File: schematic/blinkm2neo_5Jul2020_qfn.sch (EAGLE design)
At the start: 9 parts, among them IC1 ATTINY85SOIC, J1 blinkm

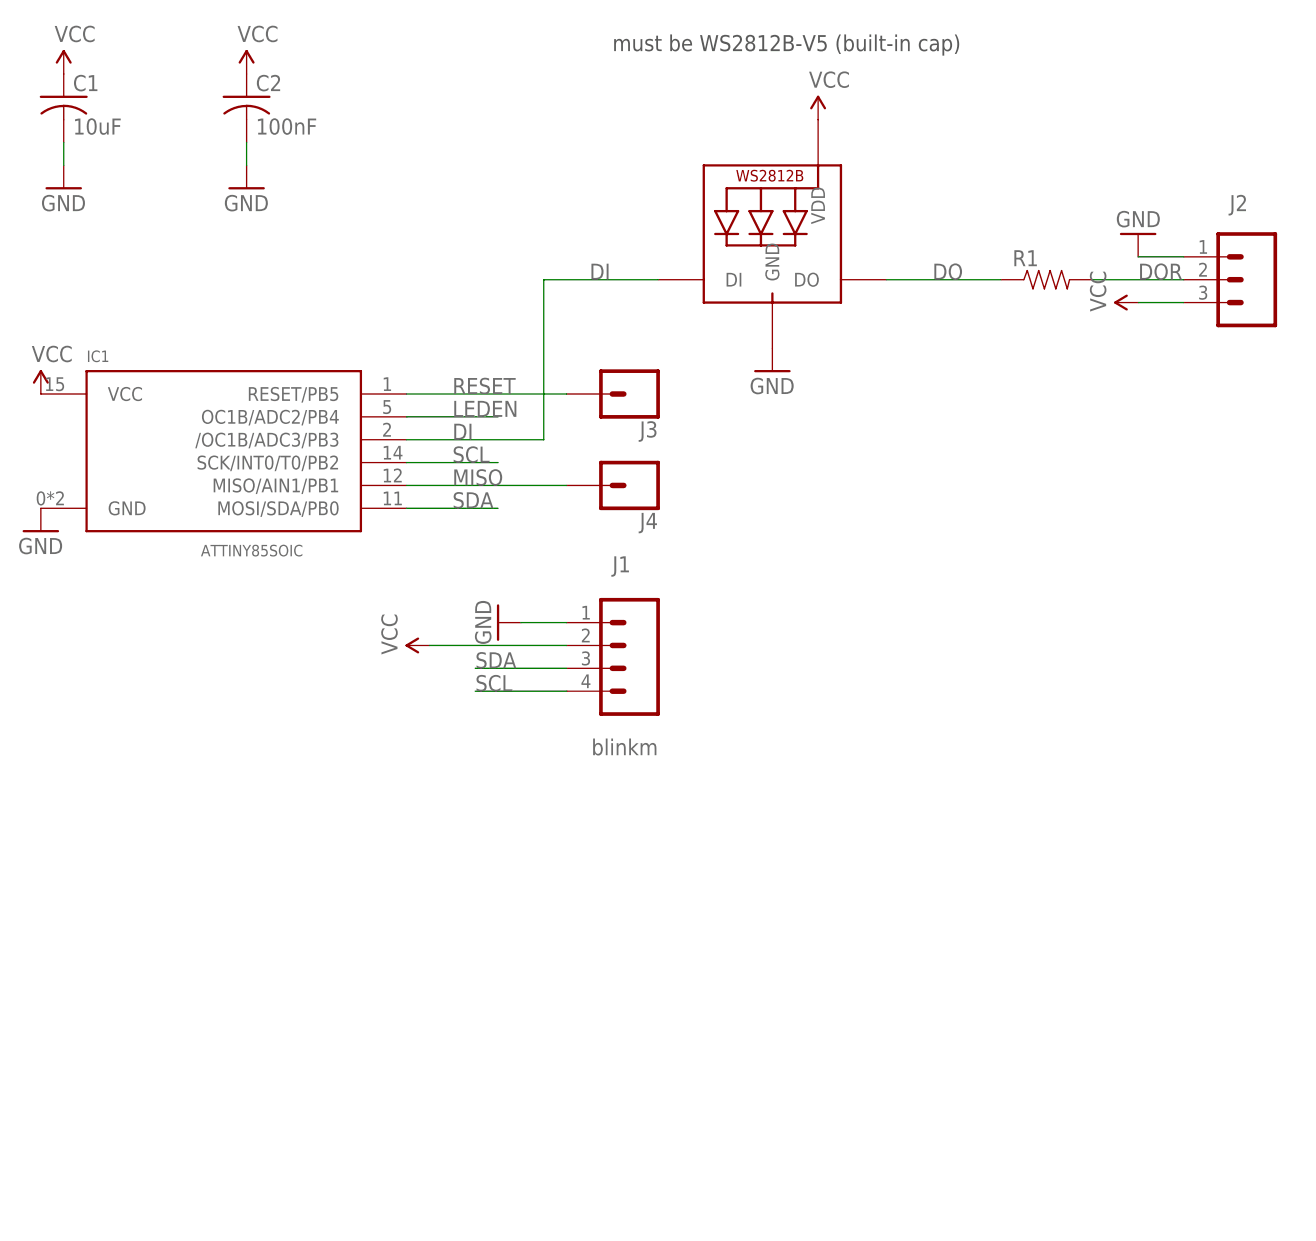
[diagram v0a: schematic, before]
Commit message: added pullup resistors
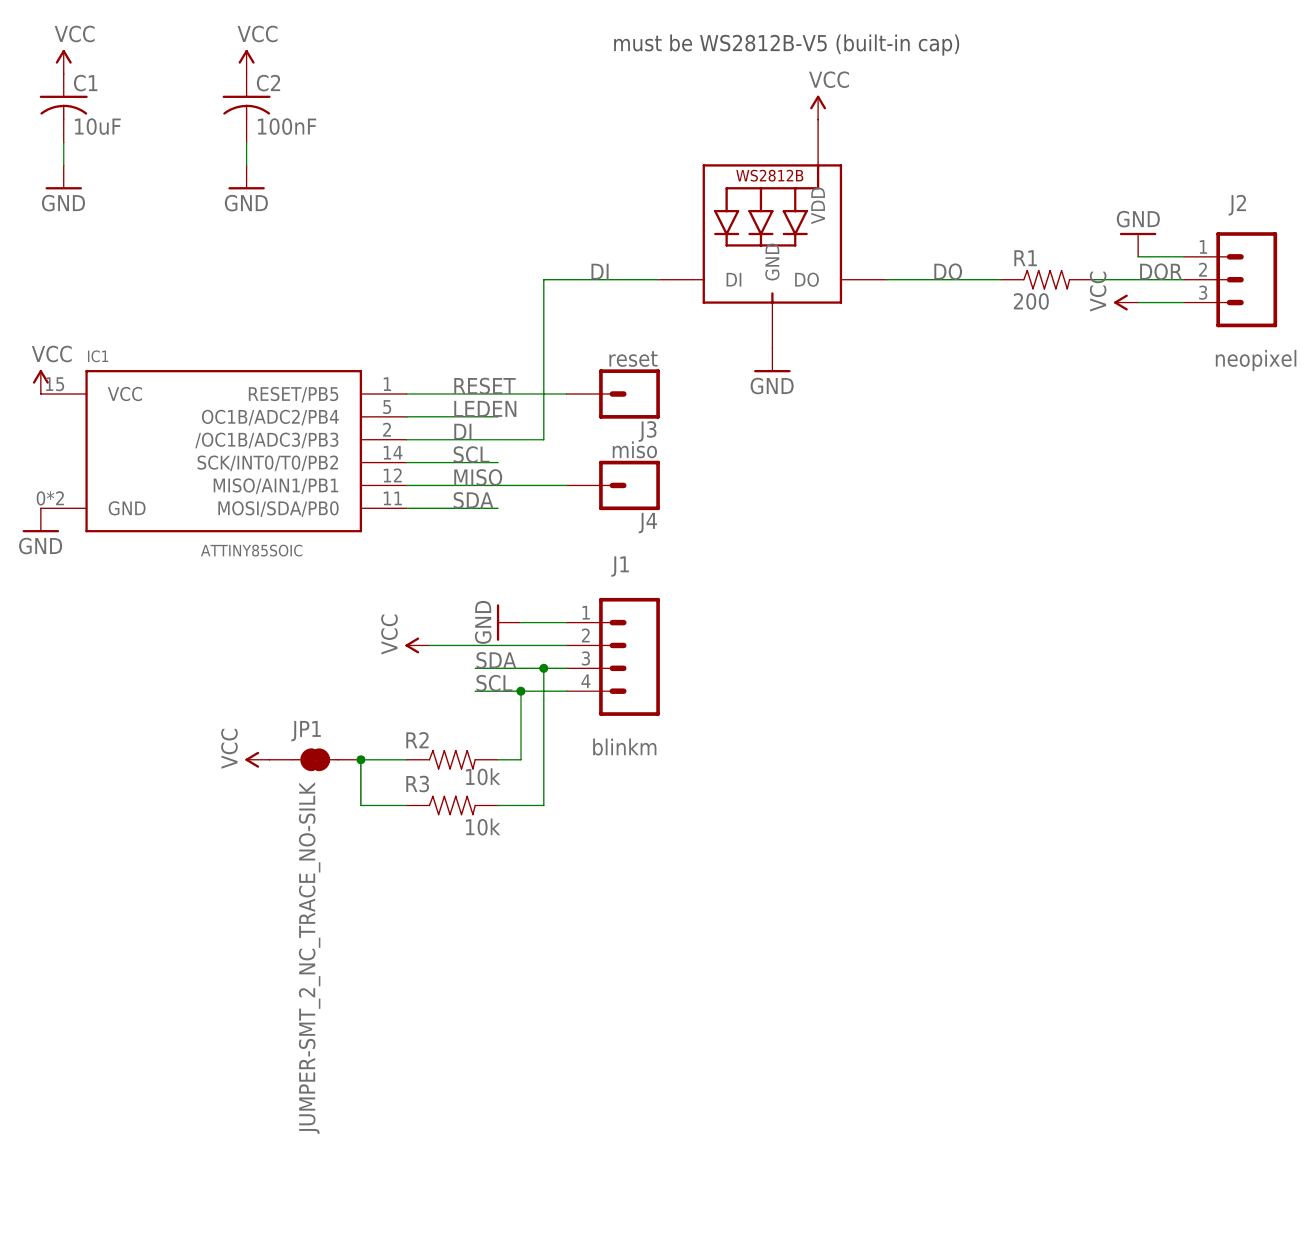
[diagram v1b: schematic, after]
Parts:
- added JP1: JUMPER-SMT_2_NC_TRACE_NO-SILK, SparkFun-Jumpers:JUMPER-SMT_2_NC_TRACE_NO-SILK
- added R2, R3: 10k, SparkFun-Resistors:RESISTOR0402
- J2: value (none) -> neopixel
- J3: value (none) -> reset
- J4: value (none) -> miso
- R1: value (none) -> 200
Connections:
- new net N$1: JP1.2, R2.1, R3.1
- net SCL: now also R2.2
- net SDA: now also R3.2
- net VCC: now also JP1.1
